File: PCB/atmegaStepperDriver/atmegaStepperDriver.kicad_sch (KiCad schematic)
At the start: 44 parts, among them J2 Screw_Terminal_01x04, Q1 TIP42C, Q2 TIP41C, Q3 TIP42C, Q4 TIP42C, Q5 TIP42C, Q6 TIP41C, Q7 TIP41C, Q8 TIP41C, U1 ATmega328P-P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

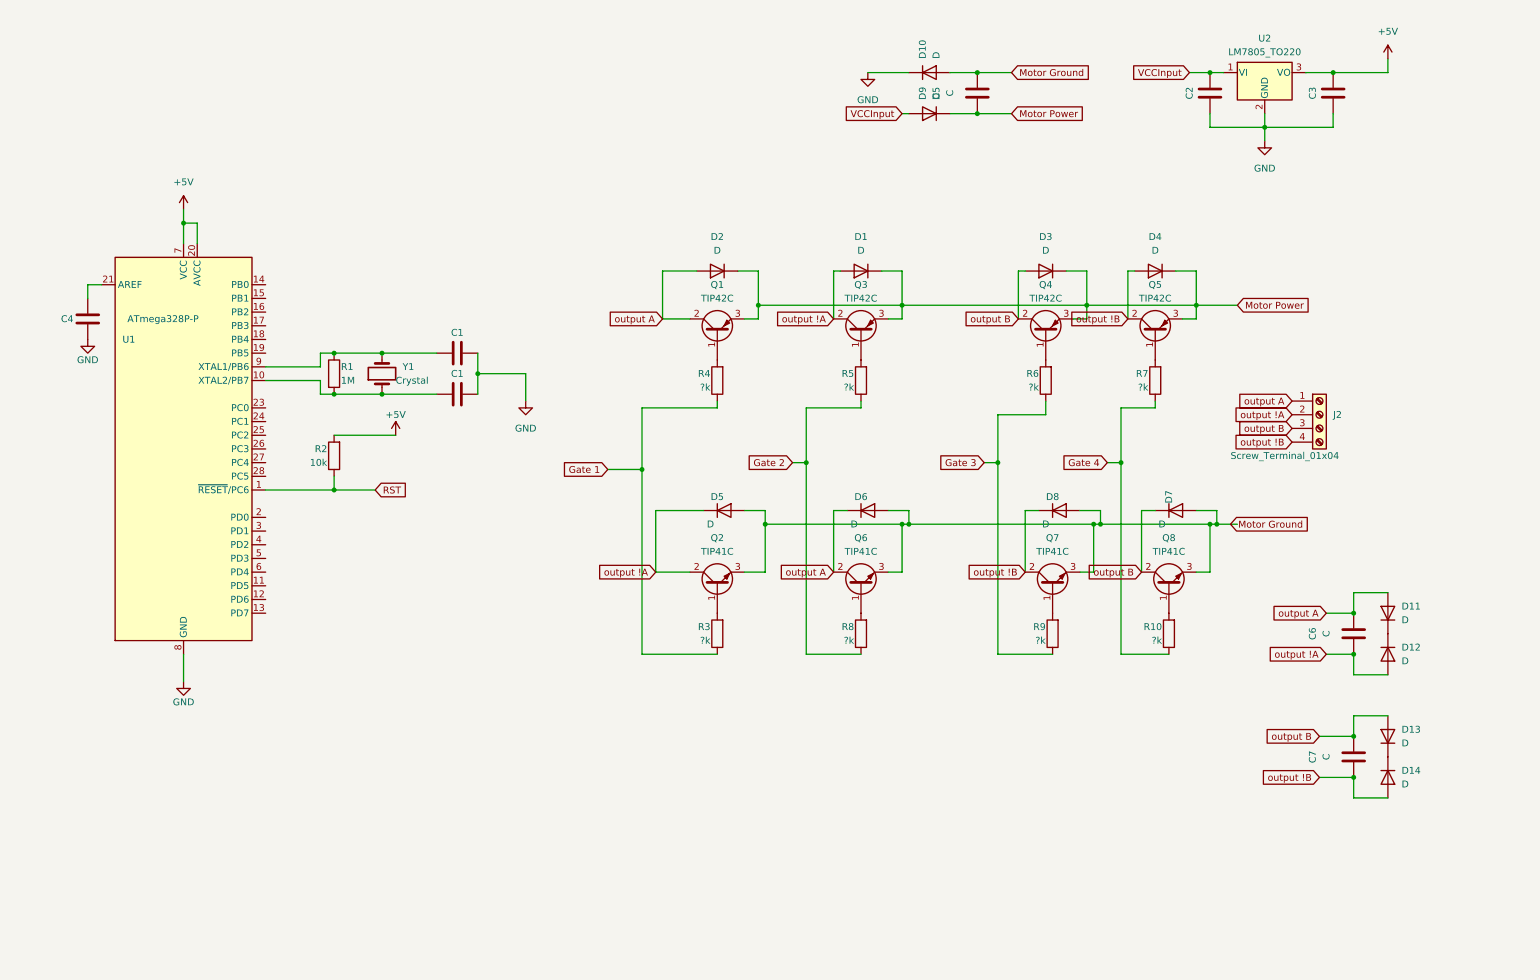
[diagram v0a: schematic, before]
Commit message: added seprate power supply box; tested protection circuit; added inputs for power;
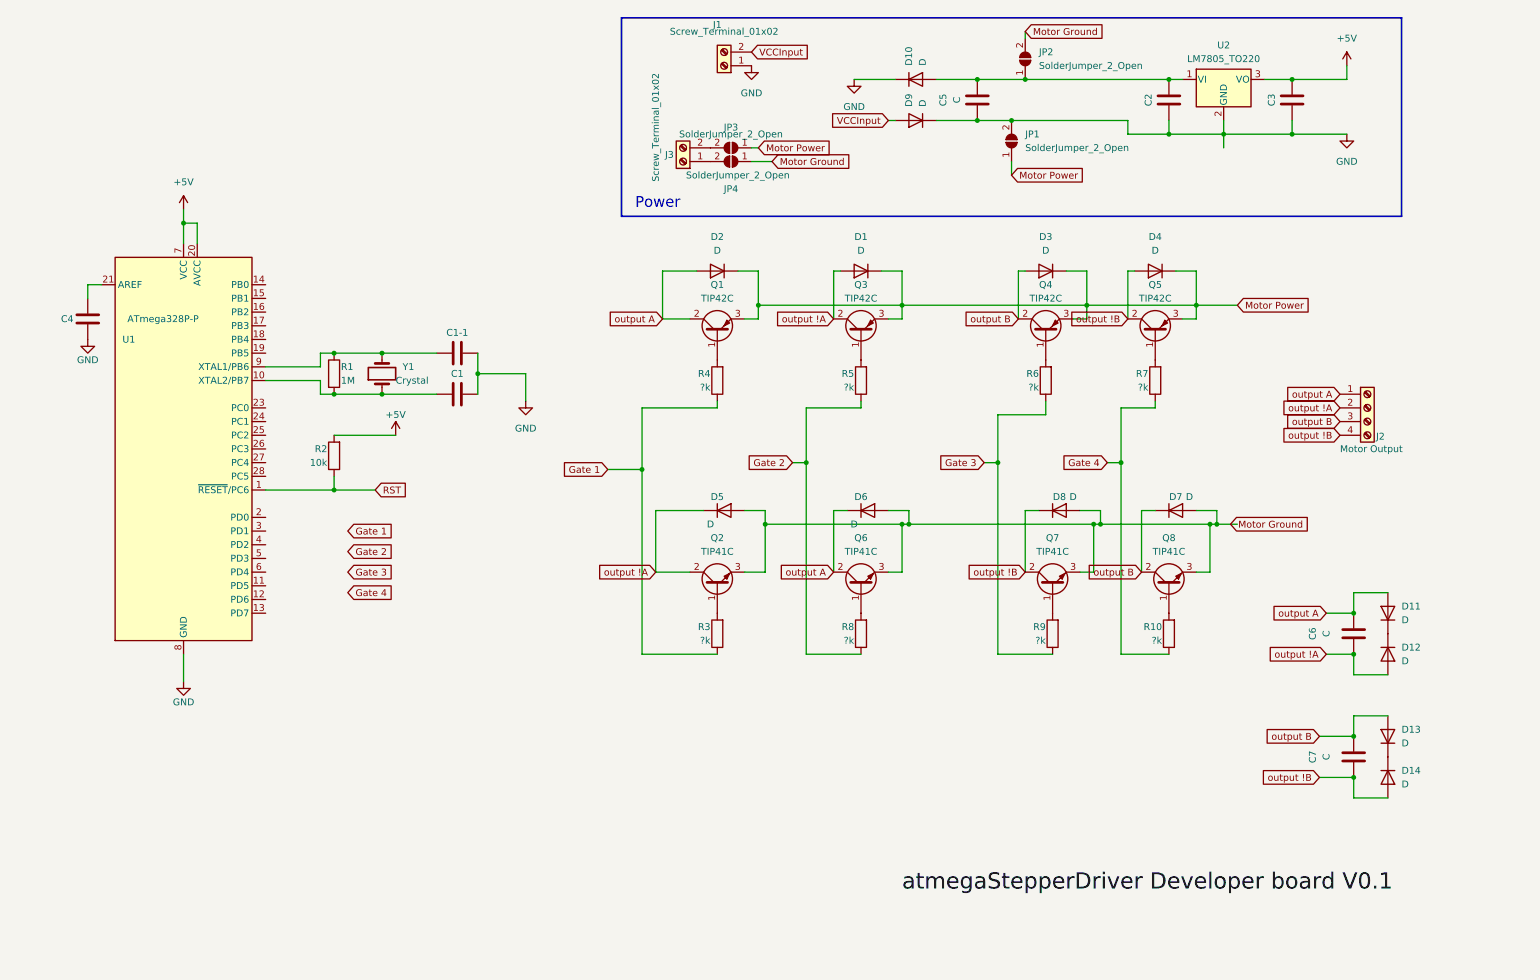
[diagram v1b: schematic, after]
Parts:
- added J1, J3: Screw_Terminal_01x02, TerminalBlock_Phoenix:TerminalBlock_Phoenix_MKDS-1,5-2_1x02_P5.00mm_Horizontal, symbol Connector:Screw_Terminal_01x02
- added JP1, JP2, JP3, JP4: SolderJumper_2_Open, Jumper:SolderJumper-2_P1.3mm_Open_RoundedPad1.0x1.5mm, symbol Jumper:SolderJumper_2_Open
- J2: value Screw_Terminal_01x04 -> Motor Output
- renumbered C1 to C1-1
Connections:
- net GND: now also C5.1, D9.1 (K), J1.1 (Pin_1), JP1.2 (B)
- net Motor Ground: now also JP2.2 (B), JP4.1 (A); no longer C5.2, D10.2 (A)
- net Motor Power: now also JP1.1 (A), JP3.1 (A); no longer C5.1, D9.1 (K)
- net VCCInput: now also J1.2 (Pin_2); no longer C2.2, U2.1 (VI)
- new net: J3.1 (Pin_1), JP4.2 (B)
- new net: C2.2, C5.2, D10.2 (A), JP2.1 (A), U2.1 (VI)
- new net: J3.2 (Pin_2), JP3.2 (B)
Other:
- note added: "Power"
- moved on the sheet: C2, C3, C5, D10, D9, J2, U2

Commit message: added programmable pins; fixed footprints; removed old protection; separated few sectors
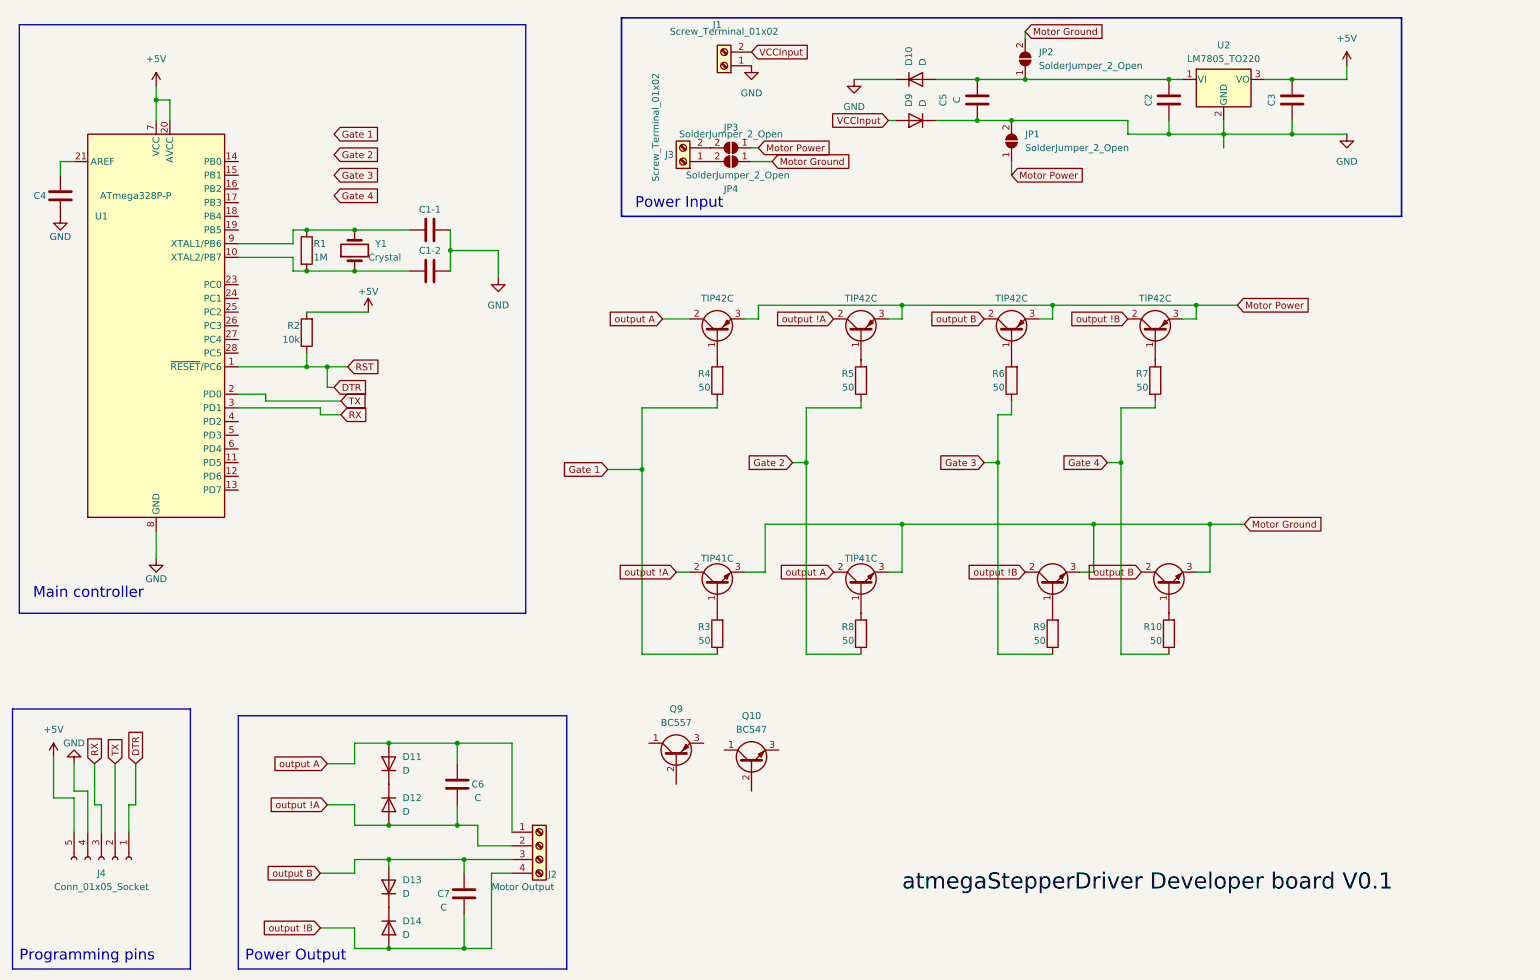
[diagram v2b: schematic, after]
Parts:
- removed D1, D2, D3, D4, D5, D6, D7, D8: D, Diode_THT:D_A-405_P7.62mm_Horizontal, symbol Device:D
- added J4: Conn_01x05_Socket, Connector_PinHeader_2.54mm:PinHeader_1x05_P2.54mm_Vertical, symbol Connector:Conn_01x05_Socket
- added Q10: BC547, Package_TO_SOT_THT:TO-92_Inline, symbol Transistor_BJT:BC547
- added Q9: BC557, Package_TO_SOT_THT:TO-92_Inline, symbol Transistor_BJT:BC557
- Q1, Q3, Q4, Q5: footprint Package_TO_SOT_THT:TO-220-3_Vertical -> Package_TO_SOT_THT:TO-220-3_Horizontal_TabDown
- R10, R3, R4, R5, R6, R7, R8, R9: value ?k -> 50
- renumbered C1 to C1-2
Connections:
- net +5V: now also J4.5 (Pin_5)
- net GND: now also J4.4 (Pin_4)
- net TX: now reaches U1.2 (PD0)
- net TX: now also J4.2 (Pin_2)
- net RX: now reaches U1.3 (PD1)
- net RX: now also J4.3 (Pin_3)
- net RST renamed DTR
- net DTR: now also J4.1 (Pin_1)
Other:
- note added: "Main controller"
- note added: "Power Input"
- note added: "Power Output"
- note added: "Programming pins"
- note removed: "Power"
- moved on the sheet: C1-1, C1-2, C4, C6, C7, D11, D12, D13, D14, J2, R1, R2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

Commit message: pcb desing started; lower level transistors added; fast pwm tested
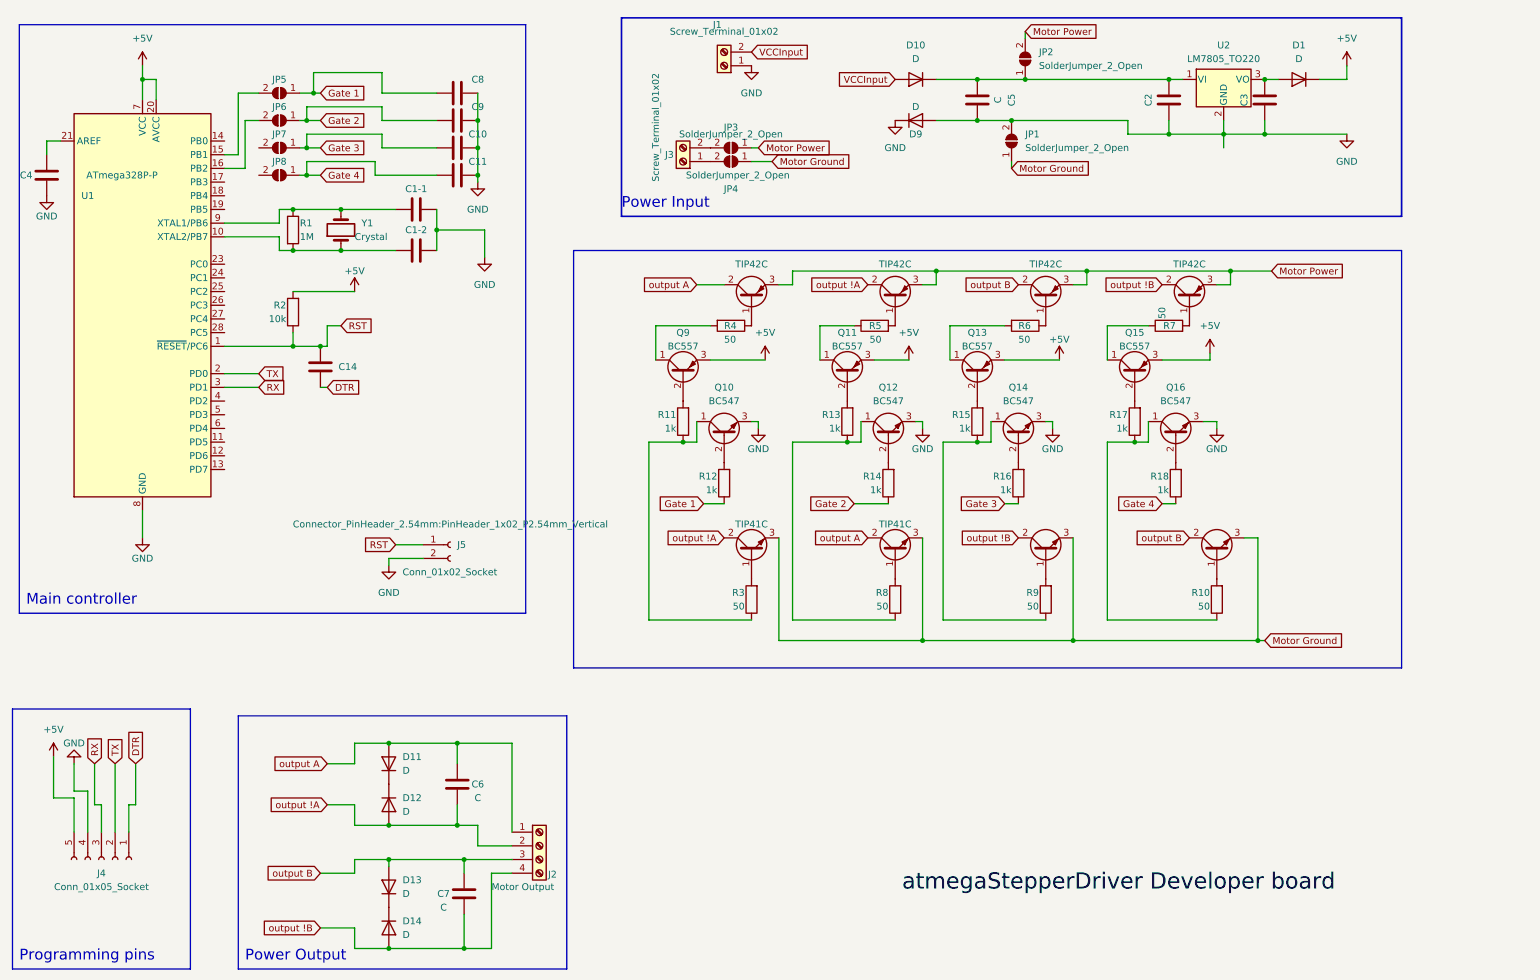
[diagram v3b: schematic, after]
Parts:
- added C10, C11, C8, C9: C, Capacitor_THT:CP_Radial_D8.0mm_P3.80mm, symbol Device:C
- added C14: C, Capacitor_THT:C_Disc_D5.0mm_W2.5mm_P2.50mm, symbol Device:C
- added D1: D, Diode_THT:D_A-405_P7.62mm_Horizontal, symbol Device:D
- added J5: Conn_01x02_Socket, Connector_PinHeader_2.54mm:PinHeader_1x02_P2.54mm_Vertical, symbol Connector:Conn_01x02_Socket
- added JP5, JP6, JP7, JP8: SolderJumper_2_Open, Jumper:SolderJumper-2_P1.3mm_Open_RoundedPad1.0x1.5mm, symbol Jumper:SolderJumper_2_Open
- added Q11, Q13, Q15: BC557, Package_TO_SOT_THT:TO-92_Inline, symbol Transistor_BJT:BC557
- added Q12, Q14, Q16: BC547, Package_TO_SOT_THT:TO-92_Inline, symbol Transistor_BJT:BC547
- added R11, R12, R13, R14, R15, R16, R17, R18: 1k, Resistor_THT:R_Axial_DIN0207_L6.3mm_D2.5mm_P10.16mm_Horizontal, symbol Device:R
- C5: footprint (none) -> Capacitor_THT:CP_Radial_Tantal_D9.0mm_P5.00mm
- C6, C7: footprint (none) -> Capacitor_THT:C_Disc_D5.0mm_W2.5mm_P2.50mm
- J2: footprint TerminalBlock_Phoenix:TerminalBlock_Phoenix_PT-1,5-4-3.5-H_1x04_P3.50mm_Horizontal -> TerminalBlock:TerminalBlock_bornier-4_P5.08mm
- Q1, Q2, Q3, Q4, Q5, Q6, Q7, Q8: footprint Package_TO_SOT_THT:TO-220-3_Horizontal_TabDown -> Package_TO_SOT_THT:TO-220-3_Vertical
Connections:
- net +5V: now also Q9.3 (E), D1.1 (K), Q11.3 (E), Q13.3 (E), Q15.3 (E); no longer C3.2, U2.3 (VO)
- net DTR: now also C14.1; no longer R2.1, U1.1 (~{RESET}/PC6)
- net GND: now also C5.2, D9.2 (A), Q10.3 (E), C10.2, C11.2, C8.2, C9.2, J5.2 (Pin_2), Q12.3 (E), Q14.3 (E), Q16.3 (E); no longer C5.1, D10.1 (K)
- net Gate 1: now also C8.1, JP5.1 (A), R12.1; no longer R3.1, R4.1
- net Gate 2: now also C9.1, JP6.1 (A), R14.1; no longer R5.1, R8.1
- net Gate 3: now also C10.1, JP7.1 (A), R16.1; no longer R6.1, R9.1
- net Gate 4: now also C11.1, JP8.1 (A), R18.1; no longer R10.1, R7.1
- net Motor Ground: now also JP1.1 (A); no longer JP2.2 (B)
- net Motor Power: now also JP2.2 (B); no longer JP1.1 (A)
- net VCCInput: now also D10.2 (A); no longer D9.2 (A)
- net at Q10.1 (C): now also R3.1, R11.1
- net at Q10.2 (B): now also R12.2
- net at C2.2, JP2.1 (A), U2.1 (VI): now also C5.1, D10.1 (K); no longer C5.2, D10.2 (A)
- net at Q1.1 (B): now also R4.1; no longer R4.2
- net at R6.2: now also Q13.1 (C); no longer Q4.1 (B)
- net at Q9.1 (C): now also R4.2
- net at Q9.2 (B): now also R11.2
- net at U1.15 (PB1): now also JP5.2 (B)
- net at U1.16 (PB2): now also JP6.2 (B)
- new net: Q13.2 (B), R15.2
- new net: Q11.1 (C), R5.1
- new net: Q14.2 (B), R16.2
- new net: Q14.1 (C), R15.1, R9.1
- new net: Q16.1 (C), R10.1, R17.1
- new net: Q15.2 (B), R17.2
- new net: Q15.1 (C), R7.1
- new net: Q16.2 (B), R18.2
- new net: Q4.1 (B), R6.1
- new net: Q12.1 (C), R13.1, R8.1
- new net: Q12.2 (B), R14.2
- new net: C3.2, D1.2 (A), U2.3 (VO)
- new net: Q11.2 (B), R13.2
- new net RST: C14.2, J5.1 (Pin_1), R2.1, U1.1 (~{RESET}/PC6)
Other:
- moved on the sheet: C1-1, C1-2, C3, C4, C5, D10, D9, Q10, Q9, R1, R10, R2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

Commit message: communication pins;
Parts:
- removed D10, D9: D, Diode_THT:D_A-405_P7.62mm_Horizontal, symbol Device:D
- added D2, D3, D4, D5: D, Diode_THT:D_A-405_P7.62mm_Horizontal, symbol Device:D
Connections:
- net GND: now also D4.2 (A); no longer J1.1 (Pin_1)
- net Motor Ground: now also D2.2 (A); no longer JP4.1 (A)
- net Motor Power: now also D3.1 (K); no longer JP3.1 (A)
- net VCCInput: now also C2.2, C5.1, JP2.1 (A), U2.1 (VI), D5.1 (K); no longer J1.2 (Pin_2)
- net Jumper To lower pisn: now reaches JP8.2 (B)
- net at JP7.2 (B): now also U1.17 (PB3)
- net Rotation: now reaches U1.13 (PD7)
- net SDA: now reaches U1.27 (PC4)
- net SCL: now reaches U1.28 (PC5)
- net Step: now reaches U1.4 (PD2)
- net Jumper To lower Pins: now reaches U1.5 (PD3)
- net Error: now reaches U1.6 (PD4)
- new net: D2.1 (K), JP4.1 (A)
- new net: D3.2 (A), JP3.1 (A)
- new net: D4.1 (K), J1.1 (Pin_1)
- new net: D5.2 (A), J1.2 (Pin_2)
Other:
- moved on the sheet: R2

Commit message: General design ready; footprints ready; V0.0.5
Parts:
- added J6: I2C Communication pins, Connector_PinHeader_2.54mm:PinHeader_1x04_P2.54mm_Vertical, symbol Connector:Conn_01x04_Pin
- added J9: Stepper communication pins, Connector_PinHeader_2.54mm:PinHeader_1x04_P2.54mm_Vertical, symbol Connector:Conn_01x04_Pin
- J1: value Screw_Terminal_01x02 -> General power
- J3: value Screw_Terminal_01x02 -> Motor power
- J5: value Conn_01x02_Socket -> Reset Header
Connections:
- net +5V: now also J6.4 (Pin_4)
- net Error: now also J9.3 (Pin_3)
- net GND: now also J6.3 (Pin_3), J9.4 (Pin_4)
- net Rotation: now also J9.2 (Pin_2)
- net SCL: now also J6.2 (Pin_2)
- net SDA: now also J6.1 (Pin_1)
- net Step: now also J9.1 (Pin_1)
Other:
- note added: "Communcation"
- note added: "Power gates"
- moved on the sheet: D4, D5, J3, J5
